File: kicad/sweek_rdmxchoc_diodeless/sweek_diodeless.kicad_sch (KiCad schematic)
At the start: 29 parts, among them J1 Conn_01x04_Socket, U1 RP2040_Zero

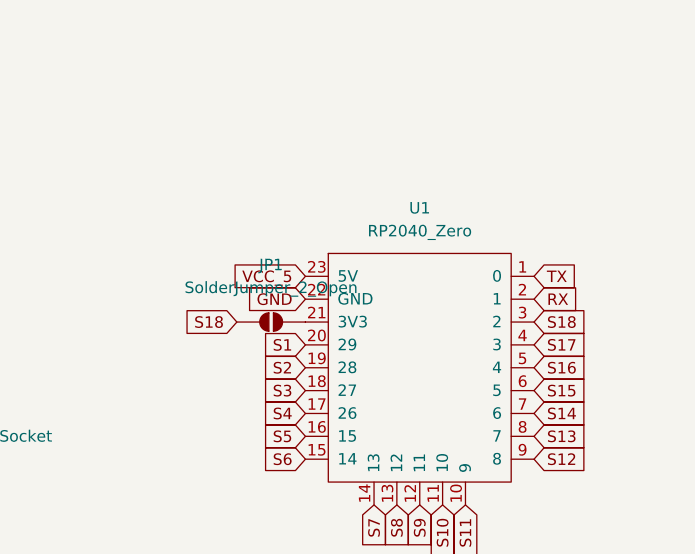
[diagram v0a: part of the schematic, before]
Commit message: Update diodeless kicad files for v1.0.1
Update diodeless kicad files for v1.0.1
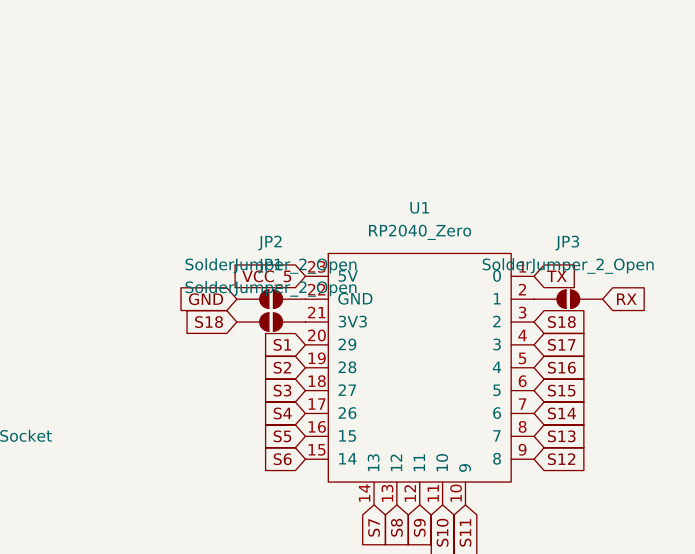
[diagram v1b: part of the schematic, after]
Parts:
- added JP2, JP3: SolderJumper_2_Open, Jumper:SolderJumper-2_P1.3mm_Open_RoundedPad1.0x1.5mm_custom, symbol Jumper:SolderJumper_2_Open
- JP1: footprint Jumper:SolderJumper-2_P1.3mm_Open_TrianglePad1.0x1.5mm -> Jumper:SolderJumper-2_P1.3mm_Open_TrianglePad1.0x1.5mm_custom
- R1, R2, R3, R4: footprint Resistor_SMD:R_1206_3216Metric_Pad1.30x1.75mm_HandSolder -> Resistor_SMD:R_1206_3216Metric_Pad1.30x1.75mm_custom
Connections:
- net GND: now also JP2.1 (A); no longer U1.22 (GND)
- net RX: now also JP3.2 (B); no longer U1.2 (1)
- new net: JP3.1 (A), U1.2 (1)
- new net: JP2.2 (B), U1.22 (GND)
